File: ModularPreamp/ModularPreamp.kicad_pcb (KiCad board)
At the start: 2 copper layers, 100 x 100 mm, 153 parts, among them J1 Barrel_Jack_Switch, J10 Conn_01x04_Male, J11 Conn_01x04_Male, J12 Conn_01x04_Male, J13 Conn_01x04_Male, J14 Conn_Coaxial, J15 Conn_Coaxial, J16 Conn_01x12_Male, J17 Conn_01x12_Male, J18 Conn_01x12_Male, J19 Conn_01x12_Male, J2 Barrel_Jack_Switch, J20 Conn_01x04_Male, J21 Conn_01x04_Male, J22 Conn_01x12_Male, J23 Screw_Terminal_01x02, J24 Screw_Terminal_01x03, J25 Screw_Terminal_01x03, J3 Screw_Terminal_01x03, J4 Conn_Coaxial, J5 Conn_01x03_Male, J6 Conn_01x12_Male, J7 Conn_01x13_Male, J8 Conn_01x12_Male, J9 Conn_01x12_Male, U1 ADA4807-4, U2 L7805, U3 L7905, U4 ADA4610-1ARJZ, U5 ADA4610-1ARJZ, U6 ADA4610-1ARJZ, U7 CenterPosGraphic, U8 CenterPosGraphic, X1 Transforme-P123_S456

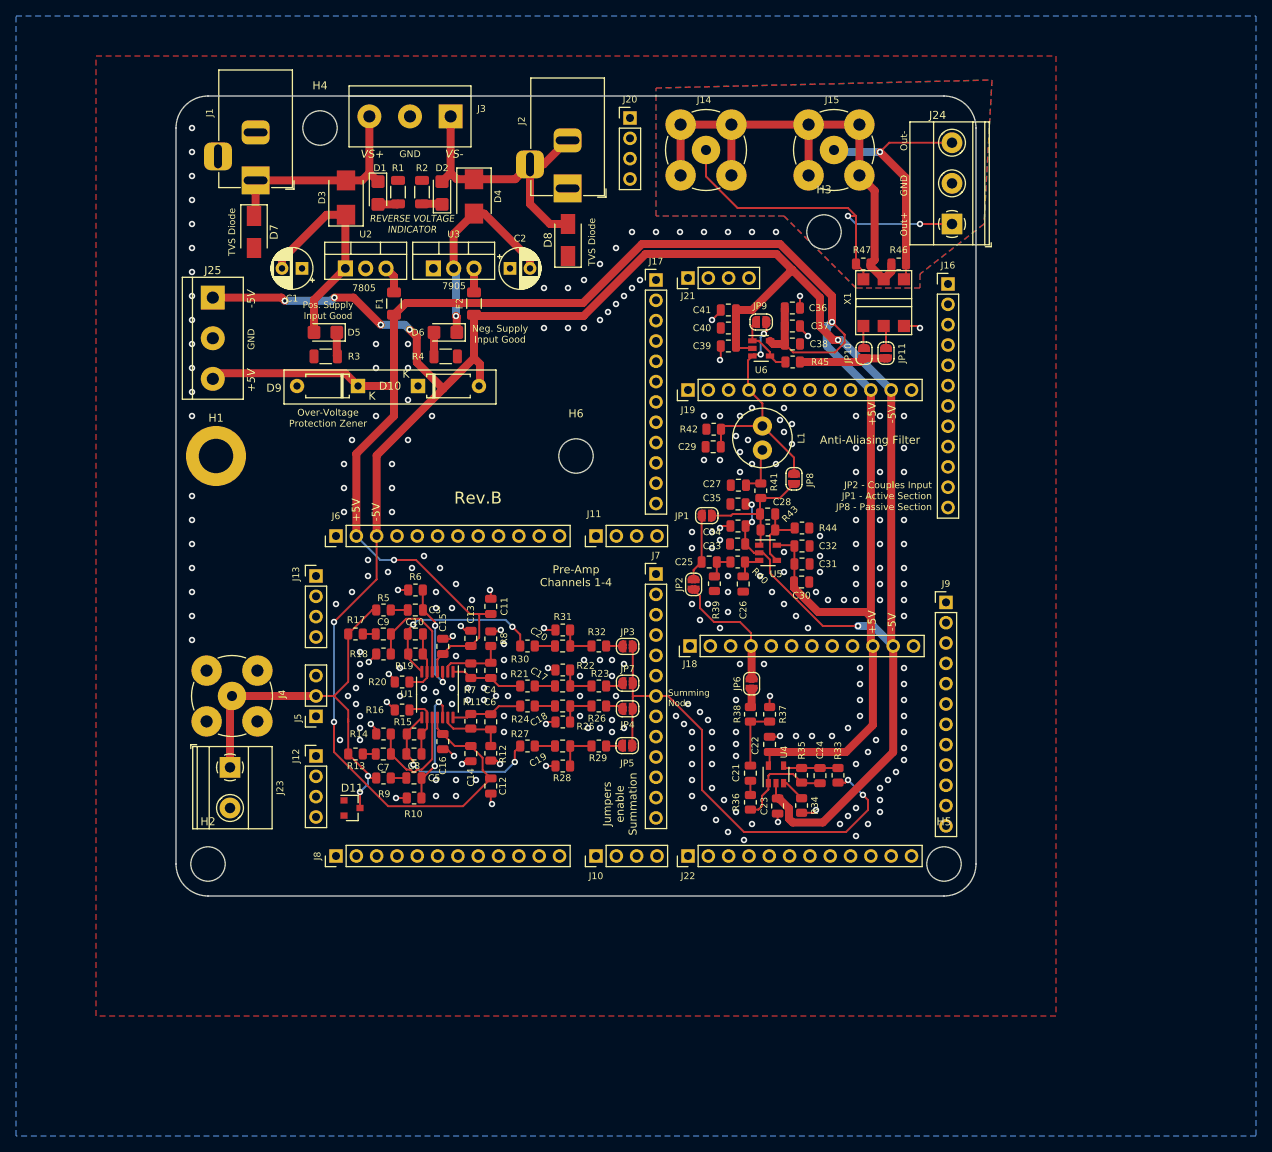
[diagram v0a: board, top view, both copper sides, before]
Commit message: Modular(JFET) preamp and INA preamp
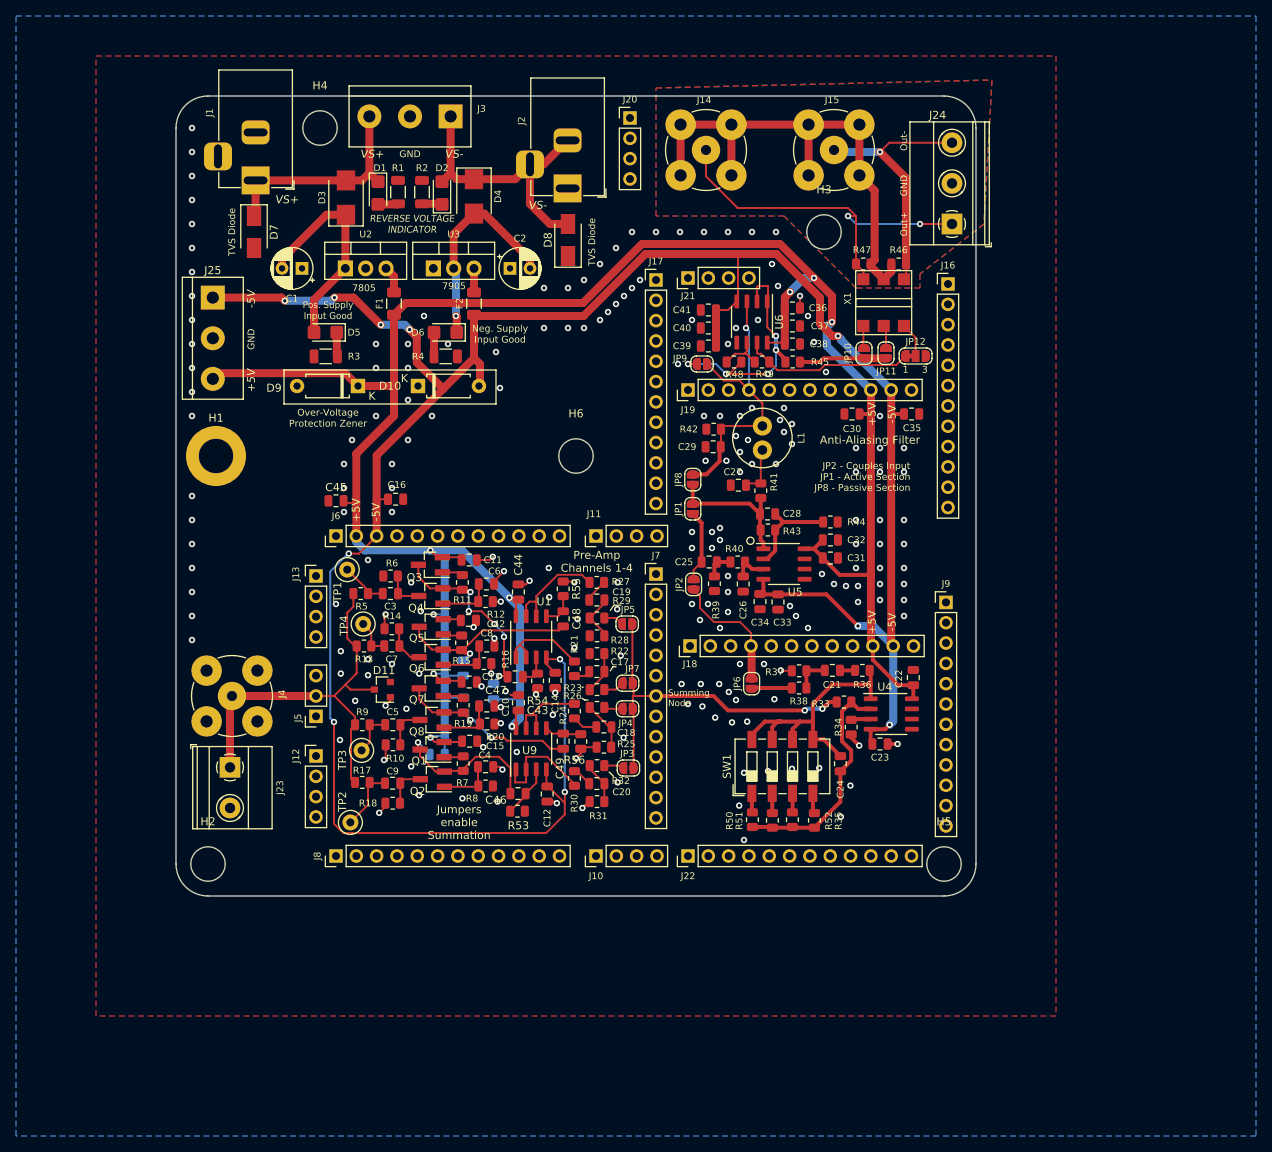
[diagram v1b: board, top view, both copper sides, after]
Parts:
- added C42: 100n, Capacitor_SMD:C_0805_2012Metric, F.Cu at (121.5, 85.5)
- added C43: 100n, Capacitor_SMD:C_0805_2012Metric, F.Cu at (127.8, 95.8)
- added C44: 100n, Capacitor_SMD:C_0805_2012Metric, F.Cu at (127.8, 82.0)
- added C45: 100n, Capacitor_SMD:C_0805_2012Metric, F.Cu at (105.0, 70.6)
- added C46: 100n, Capacitor_SMD:C_0805_2012Metric, F.Cu at (127.8, 107.2)
- added C47: 100n, Capacitor_SMD:C_0805_2012Metric, F.Cu at (127.4, 92.6)
- added C48: 100n, Capacitor_SMD:C_0805_2012Metric, F.Cu at (133.4, 85.3)
- added C49: 100n, Capacitor_SMD:C_0805_2012Metric, F.Cu at (133.4, 100.7)
- added C50: 100p, Capacitor_SMD:C_0805_2012Metric, B.Cu at (117.7, 102.3)
- added C51: 100p, Capacitor_SMD:C_0805_2012Metric, B.Cu at (124.7, 94.5)
- added C52: 100p, Capacitor_SMD:C_0805_2012Metric, B.Cu at (120.9, 91.5)
- added C53: 100p, Capacitor_SMD:C_0805_2012Metric, B.Cu at (121.0, 96.2)
- added JP12: SolderJumper_3_Bridged12, Jumper:SolderJumper-3_P1.3mm_Bridged12_RoundedPad1.0x1.5mm_NumberLabels, F.Cu at (177.4, 52.5)
- added Q1: Q_NJFET_SDG, Package_TO_SOT_SMD:SOT-23_Handsoldering, F.Cu at (117.0, 101.7)
- added Q2: Q_NJFET_SDG, Package_TO_SOT_SMD:SOT-23_Handsoldering, F.Cu at (117.0, 105.4)
- added Q3: Q_NJFET_SDG, Package_TO_SOT_SMD:SOT-23_Handsoldering, F.Cu at (116.8, 78.6)
- added Q4: Q_NJFET_SDG, Package_TO_SOT_SMD:SOT-23_Handsoldering, F.Cu at (116.8, 82.5)
- added Q5: Q_NJFET_SDG, Package_TO_SOT_SMD:SOT-23_Handsoldering, F.Cu at (116.9, 86.3)
- added Q6: Q_NJFET_SDG, Package_TO_SOT_SMD:SOT-23_Handsoldering, F.Cu at (116.9, 90.2)
- added Q7: Q_NJFET_SDG, Package_TO_SOT_SMD:SOT-23_Handsoldering, F.Cu at (116.9, 94.0)
- added Q8: Q_NJFET_SDG, Package_TO_SOT_SMD:SOT-23_Handsoldering, F.Cu at (117.0, 98.0)
- added R48: 1k, Resistor_SMD:R_0805_2012Metric, F.Cu at (154.8, 53.2)
- added R49: 1k, Resistor_SMD:R_0805_2012Metric, F.Cu at (158.2, 53.2)
- added R50: 100, Resistor_SMD:R_0805_2012Metric, F.Cu at (157.1, 110.5)
- added R51: 470, Resistor_SMD:R_0805_2012Metric, F.Cu at (159.6, 110.5)
- added R52: 1k, Resistor_SMD:R_0805_2012Metric, F.Cu at (162.1, 110.5)
- added R53: 10k, Resistor_SMD:R_0805_2012Metric, F.Cu at (127.7, 109.4)
- added R54: 10k, Resistor_SMD:R_0805_2012Metric, F.Cu at (130.2, 93.1)
- added R55: 10k, Resistor_SMD:R_0805_2012Metric, F.Cu at (133.4, 81.6)
- added R56: 10k, Resistor_SMD:R_0805_2012Metric, F.Cu at (135.6, 100.7)
- added SW1: SW_DIP_x04, Button_Switch_SMD:SW_DIP_SPSTx04_Slide_6.7x11.72mm_W6.73mm_P2.54mm_LowProfile_JPin, F.Cu at (160.8, 103.8)
- added TP1: TestPoint, TestPoint:TestPoint_Loop_D1.80mm_Drill1.0mm_Beaded, F.Cu at (106.4, 79.2)
- added TP2: TestPoint, TestPoint:TestPoint_Loop_D1.80mm_Drill1.0mm_Beaded, F.Cu at (106.8, 110.8)
- added TP3: TestPoint, TestPoint:TestPoint_Loop_D1.80mm_Drill1.0mm_Beaded, F.Cu at (108.2, 101.8)
- added TP4: TestPoint, TestPoint:TestPoint_Loop_D1.80mm_Drill1.0mm_Beaded, F.Cu at (108.4, 86.0)
- added U9: ADA4075-2, Package_SO:SO-8_3.9x4.9mm_P1.27mm, F.Cu at (129.4, 101.6)
- C10, C4, C6, C8: value 220p -> 10u
- C11: value 1u -> 100n
- C15, C17, C18, C19, C20, C3, C5, C7, C9: value 1n -> 100n
- R10, R14, R18, R6: value 10k -> 100k
- R11, R15, R19, R7: value 1k -> 10
- R12, R16, R20, R8: value 47 -> 10
- R13, R17, R24, R27, R9: value 0 -> DNP
- R32: value 47 -> DNP
- R35: value 1k -> 4.7k
- U1: value ADA4807-4 -> ADA4075-2; footprint Package_SO:TSSOP-14_4.4x5mm_P0.65mm -> Package_SO:SO-8_3.9x4.9mm_P1.27mm
- U4, U5, U6: value ADA4610-1ARJZ -> ADA4075-2; footprint Package_TO_SOT_SMD:SOT-23-5 -> Package_SO:SO-8_3.9x4.9mm_P1.27mm
- moved C16 30.9 mm to (112.5, 70.4), turned to 180 degrees
- moved C35 24.4 mm to (176.9, 59.8), turned to 180 degrees
- moved R27 22.2 mm to (137.6, 80.8)
- moved C30 21.9 mm to (169.5, 59.8), turned to 0 degrees
- moved R31 21.9 mm to (137.6, 108.2)
- moved R36 21.6 mm to (170.8, 91.8), turned to 0 degrees
- moved C22 19.8 mm to (177.2, 92.7)
- moved R12 19.0 mm to (123.7, 83.2), turned to 0 degrees
- moved C19 18.7 mm to (137.6, 83.0)
- moved C9 18.7 mm to (112.1, 105.9)
- moved R18 18.7 mm to (112.1, 108.4)
- moved R17 18.6 mm to (108.3, 105.8)
- moved R8 18.4 mm to (123.7, 106.2), turned to 0 degrees
- moved C20 17.7 mm to (137.6, 106.0)
- moved R30 17.6 mm to (134.8, 105.3), turned to -90 degrees
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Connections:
- C10 pad 2: Net-(C10-Pad2) -> GND
- C4 pad 2: Net-(C4-Pad2) -> GND
- C6 pad 2: Net-(C6-Pad2) -> GND
- C8 pad 2: Net-(C8-Pad2) -> GND
- J25 pad 2: Net-(J25-Pad2) -> GND
- R11 pad 1: Net-(C6-Pad1) -> Net-(Q3-Pad1)
- R11 pad 2: Net-(C6-Pad2) -> Net-(C47-Pad2)
- R12 pad 1: GND -> Net-(C6-Pad1)
- R12 pad 2: Net-(C6-Pad1) -> GND
- R15 pad 1: Net-(C8-Pad1) -> Net-(Q5-Pad1)
- R15 pad 2: Net-(C8-Pad2) -> Net-(C48-Pad2)
- R16 pad 1: GND -> Net-(C8-Pad1)
- R16 pad 2: Net-(C8-Pad1) -> GND
- R19 pad 1: Net-(C10-Pad1) -> Net-(Q7-Pad1)
- R19 pad 2: Net-(C10-Pad2) -> Net-(C49-Pad2)
- R20 pad 1: GND -> Net-(C10-Pad1)
- R20 pad 2: Net-(C10-Pad1) -> GND
- R21 pad 2: Net-(C4-Pad2) -> Net-(R21-Pad2)
- R24 pad 2: Net-(C6-Pad2) -> Net-(R24-Pad2)
- R27 pad 2: Net-(C8-Pad2) -> Net-(R27-Pad2)
- R30 pad 2: Net-(C10-Pad2) -> Net-(R30-Pad2)
- R35 pad 1: Net-(C24-Pad1) -> Net-(R35-Pad1)
- R7 pad 1: Net-(C4-Pad1) -> Net-(Q1-Pad1)
- R7 pad 2: Net-(C4-Pad2) -> Net-(C46-Pad2)
- R8 pad 1: GND -> Net-(C4-Pad1)
- R8 pad 2: Net-(C4-Pad1) -> GND
- U1 pad 1: Net-(C4-Pad2) -> Net-(R21-Pad2)
- U1 pad 2: Net-(C4-Pad1) -> Net-(R21-Pad2)
- U1 pad 3: Net-(C3-Pad1) -> Net-(C47-Pad1)
- U1 pad 4: +5V -> -5V
- U1 pad 5: Net-(C9-Pad1) -> Net-(C48-Pad1)
- U1 pad 6: Net-(C10-Pad1) -> Net-(R27-Pad2)
- U1 pad 7: Net-(C10-Pad2) -> Net-(R27-Pad2)
- U1 pad 8: Net-(C8-Pad2) -> +5V
- U4 pad 2: -5V -> Net-(C24-Pad2)
- U4 pad 4: Net-(C24-Pad2) -> -5V
- U4 pad 5: +5V -> (no net)
- U5 pad 2: -5V -> Net-(C28-Pad1)
- U5 pad 4: Net-(C28-Pad1) -> -5V
- U5 pad 5: +5V -> (no net)
- U6 pad 2: -5V -> Net-(JP9-Pad2)
- U6 pad 4: Net-(JP9-Pad2) -> -5V
- U6 pad 5: +5V -> GND
- X1 pad 3: GND -> Net-(JP12-Pad2)
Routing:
- net +5V: track 255.3 -> 299.0 mm, vias 2 -> 9
- net Net-(C47-Pad2): track 0.00 -> 24.8 mm, vias 0 -> 5
- net Net-(C48-Pad2): track 0.00 -> 23.6 mm, vias 0 -> 1
- net Net-(JP9-Pad2): track 8.04 -> 31.3 mm, vias 0 -> 5
- net Net-(C49-Pad2): track 0.00 -> 23.2 mm, vias 0 -> 2
- net Net-(C8-Pad2): track 22.9 -> 0.00 mm, vias 2 -> 0
- net Net-(C10-Pad2): track 22.4 -> 0.00 mm, vias 2 -> 0
- net Net-(C24-Pad2): track 6.92 -> 29.2 mm
- net Net-(C24-Pad1): track 12.8 -> 35.0 mm
- net Net-(JP12-Pad1): track 0.00 -> 21.4 mm
- net Net-(C46-Pad2): track 0.00 -> 20.7 mm, vias 0 -> 1
- net Sum: track 60.6 -> 46.2 mm
- net Net-(R30-Pad2): track 0.00 -> 13.9 mm
- net Net-(R27-Pad2): track 0.00 -> 13.5 mm
- net Net-(R21-Pad2): track 0.00 -> 11.8 mm
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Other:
- net class Default removed
- board text added: "Rev.B 20FEB2023 E. Mattingly"
- board text removed: "Rev.B"
